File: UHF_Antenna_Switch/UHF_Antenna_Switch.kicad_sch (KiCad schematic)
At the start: 27 parts, among them J1 Conn_N_Type_Female, J2 Conn_SO-239, J3 Conn_SMA_Female, J4 Screw_Terminal_01x02, SW1 SW_SP3T, U1 LTC5507ES6, U2 PAT1220-C-10DB, U3 X4C09F1-30S, U4 RP2040-Zero

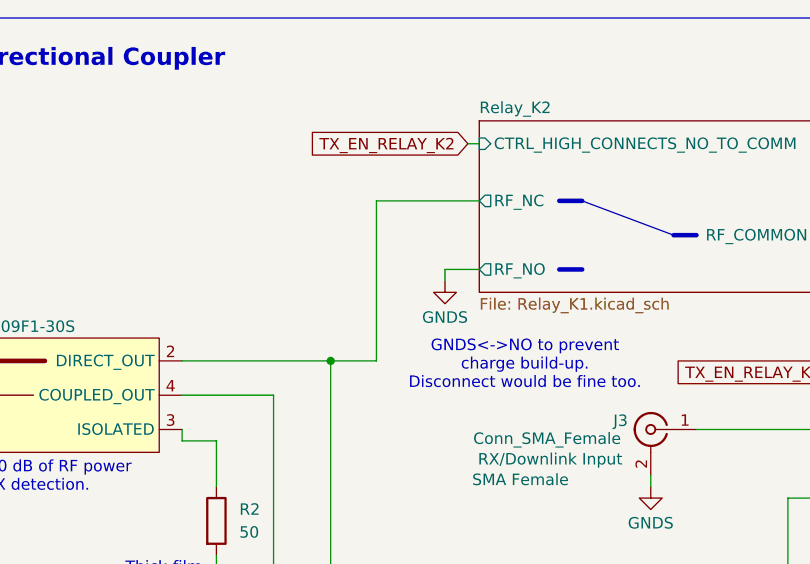
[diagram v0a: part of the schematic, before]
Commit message: Configure net classes and trace widths
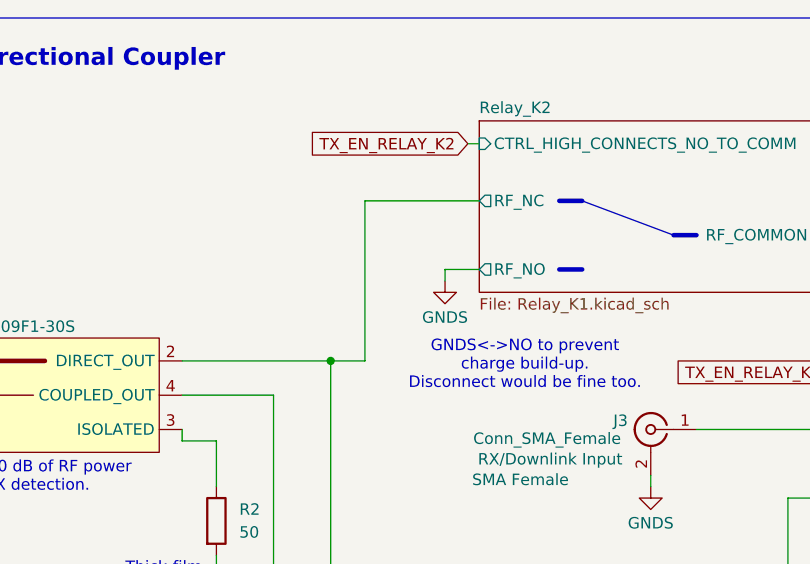
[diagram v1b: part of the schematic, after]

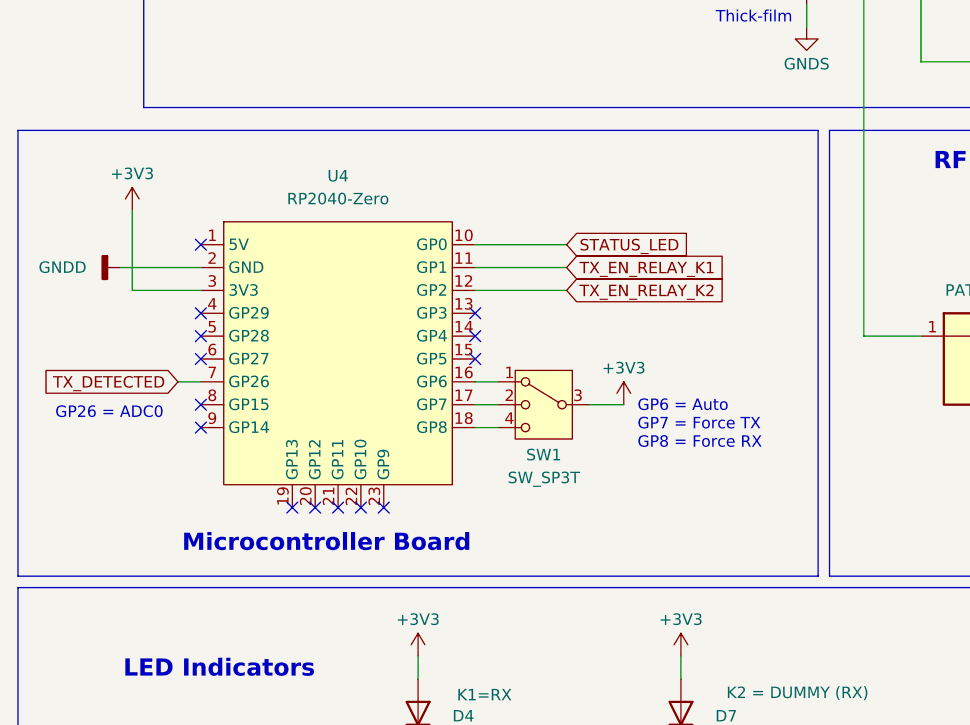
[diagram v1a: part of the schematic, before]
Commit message: Complete initial positioning of components (no routing)
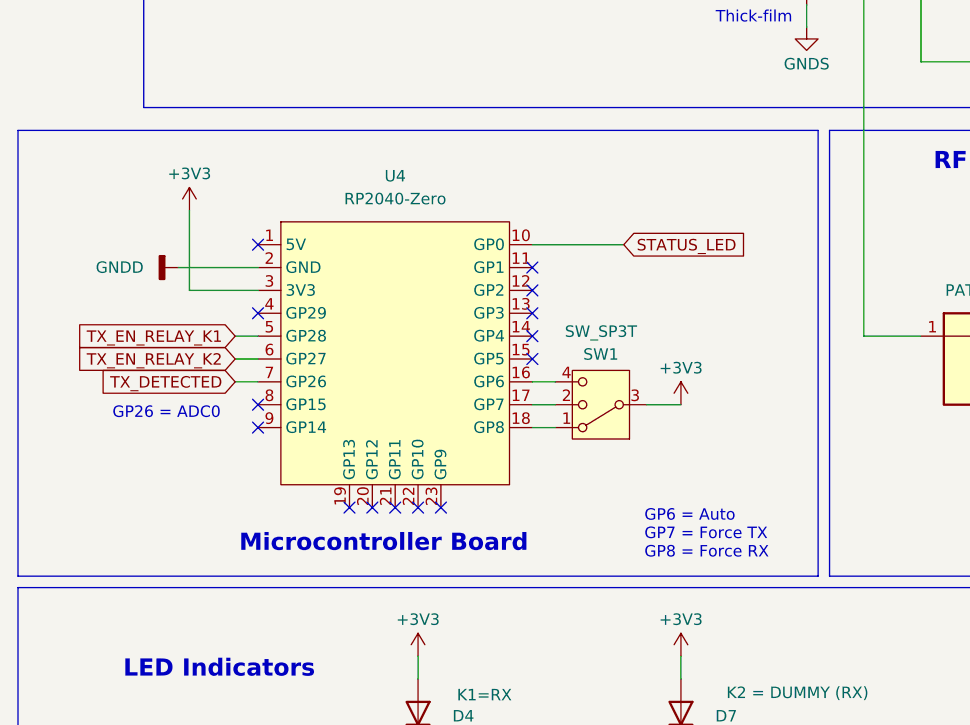
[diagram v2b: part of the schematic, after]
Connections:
- net TX_EN_RELAY_K1: now also U4.5 (GP28); no longer U4.11 (GP1)
- net TX_EN_RELAY_K2: now also U4.6 (GP27); no longer U4.12 (GP2)
- net at U4.16 (GP6): now also SW1.4; no longer SW1.1
- net at U4.18 (GP8): now also SW1.1; no longer SW1.4
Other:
- moved on the sheet: SW1, U4

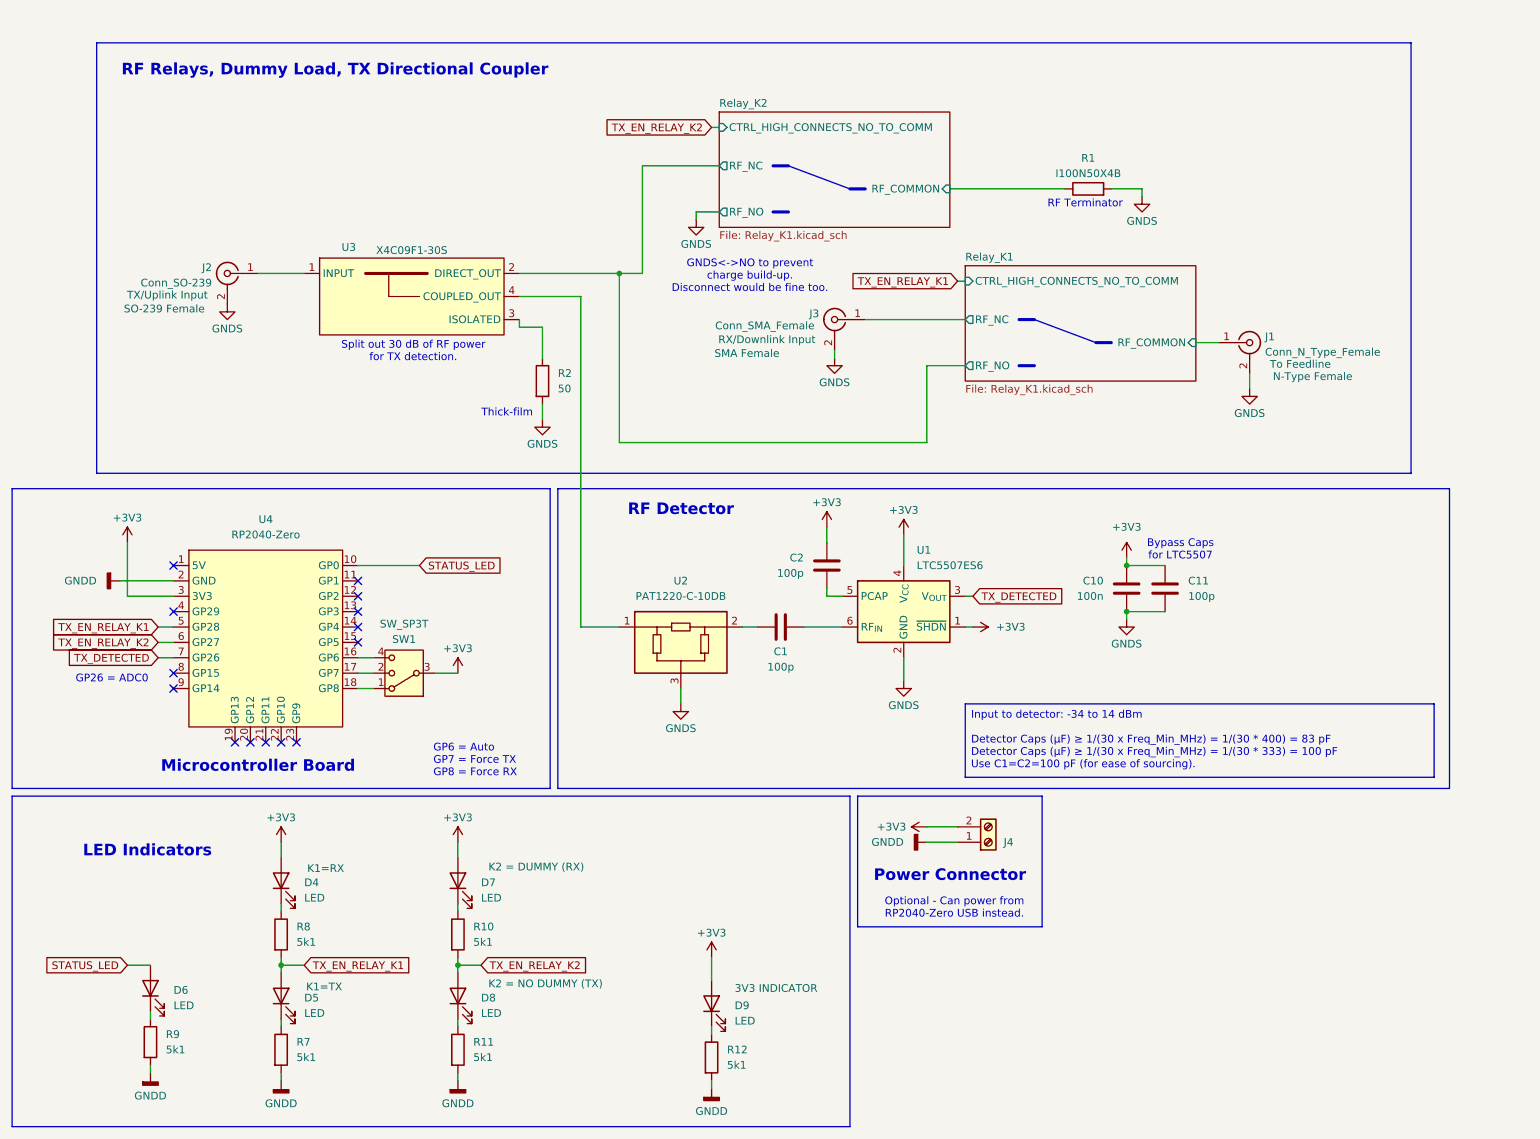
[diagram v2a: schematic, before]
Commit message: Schematic: Add PTT switches, PTT header, 5V power screw
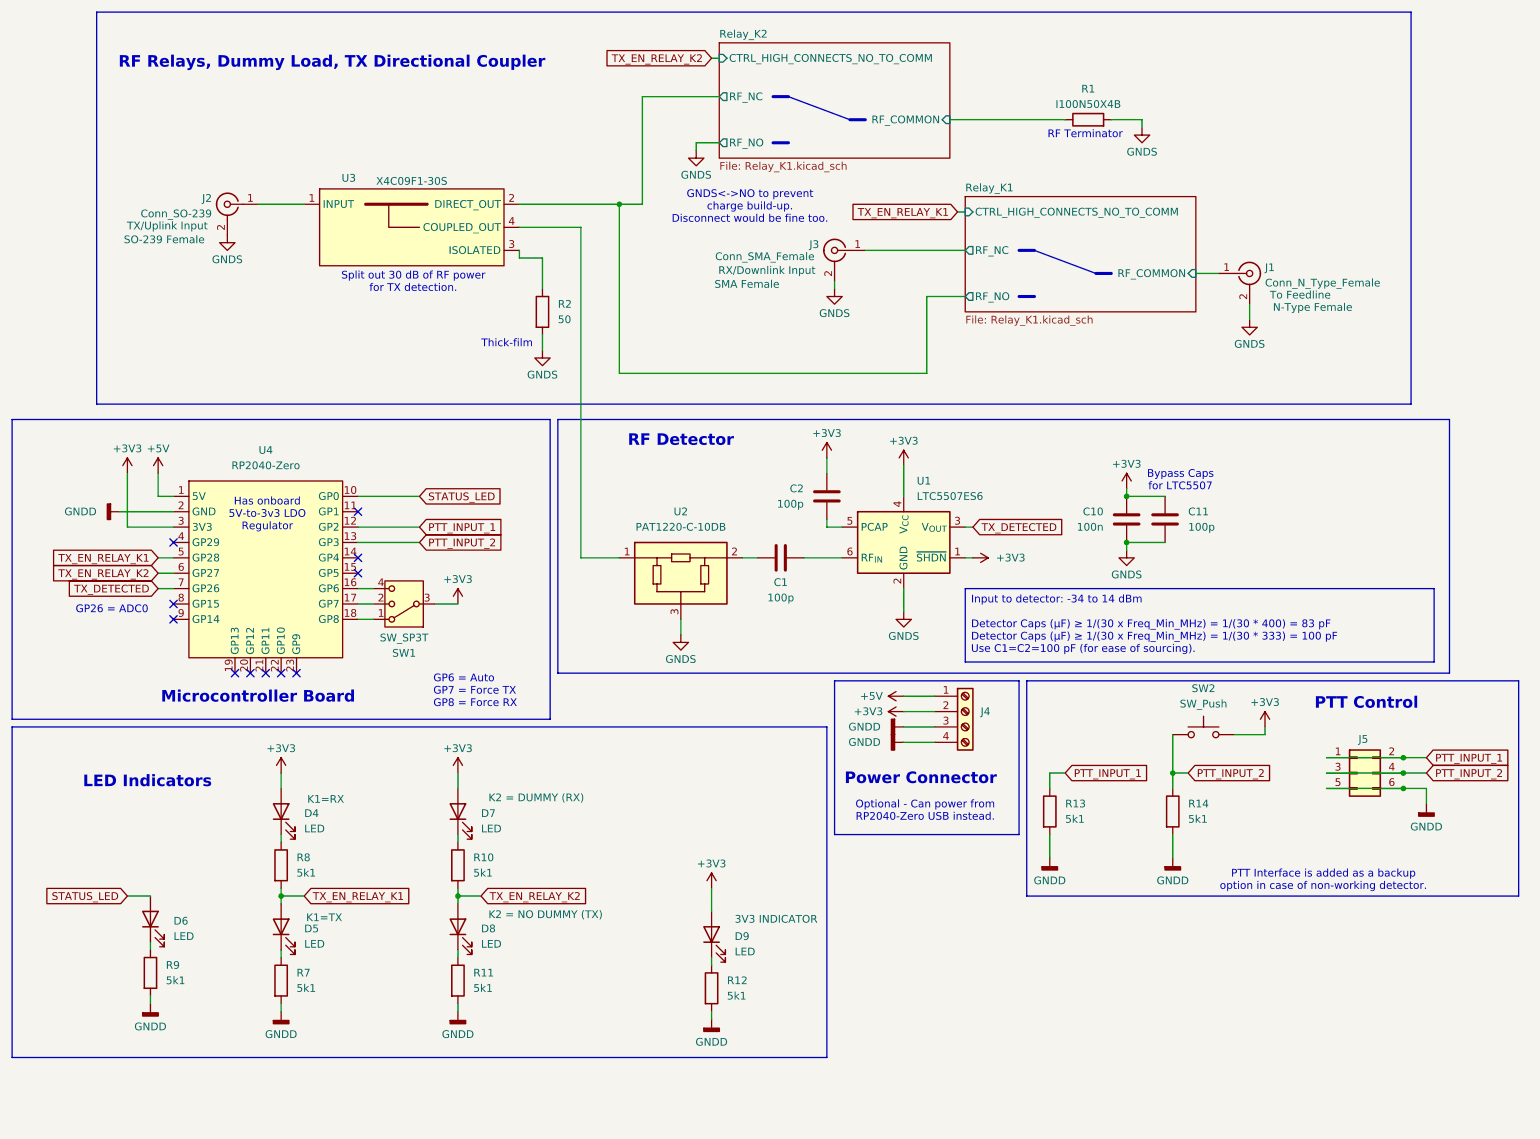
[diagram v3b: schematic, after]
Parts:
- removed J4: Screw_Terminal_01x02, TerminalBlock_Phoenix:TerminalBlock_Phoenix_MKDS-3-2-5.08_1x02_P5.08mm_Horizontal, symbol Connector:Screw_Terminal_01x02
- added J4: Screw_Terminal_01x04, TerminalBlock_Phoenix:TerminalBlock_Phoenix_MKDS-1,5-4-5.08_1x04_P5.08mm_Horizontal, symbol Connector:Screw_Terminal_01x04
- added J5: Conn_02x03_Odd_Even, Connector_PinHeader_2.54mm:PinHeader_2x03_P2.54mm_Vertical, symbol Connector_Generic:Conn_02x03_Odd_Even
- added R13, R14: 5k1, Resistor_SMD:R_0603_1608Metric_Pad0.98x0.95mm_HandSolder, symbol Device:R
- added SW2: SW_Push, Button_Switch_THT:SW_PUSH_6mm_H4.3mm, symbol Switch:SW_Push
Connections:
- net +3V3: now also J4.2 (Pin_2), SW2.2
- net GNDD: now also J4.3 (Pin_3), J4.4 (Pin_4), J5.5 (Pin_5), J5.6 (Pin_6), R13.2, R14.2
- net +5V: now reaches U4.1 (5V)
- net +5V: now also J4.1 (Pin_1)
- net PTT_INPUT_1: now reaches U4.12 (GP2)
- net PTT_INPUT_1: now also J5.1 (Pin_1), J5.2 (Pin_2), R13.1
- net PTT_INPUT_2: now reaches U4.13 (GP3)
- net PTT_INPUT_2: now also J5.3 (Pin_3), J5.4 (Pin_4), R14.1, SW2.1
- no-connect marks 14 -> 11
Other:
- note added: "Has onboard 5V-to-3v3 LDO Regulator"
- note added: "PTT Control"
- note added: "PTT Interface is added as a backup option in case of non-working detector."
- moved on the sheet: C1, C10, C11, C2, D4, D5, D6, D7, D8, D9, J1, J2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

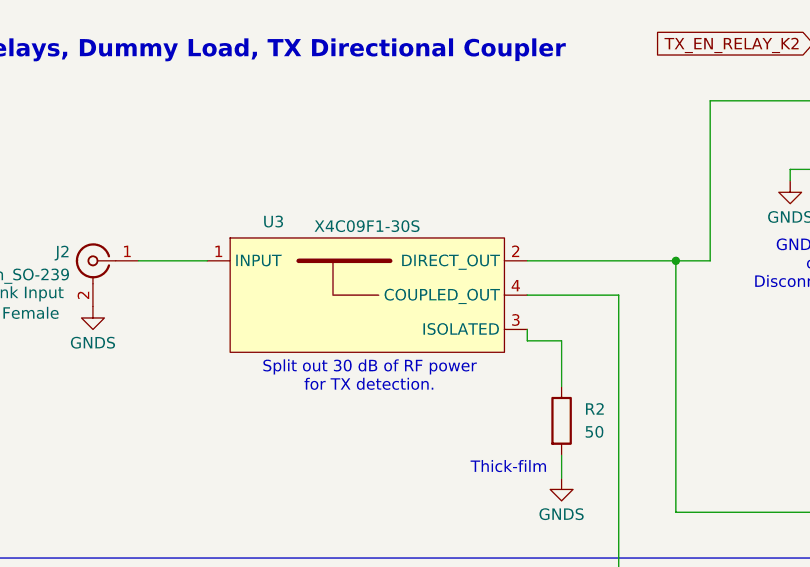
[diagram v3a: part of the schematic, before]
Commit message: Footprint: Draw RF coupler with microstrip
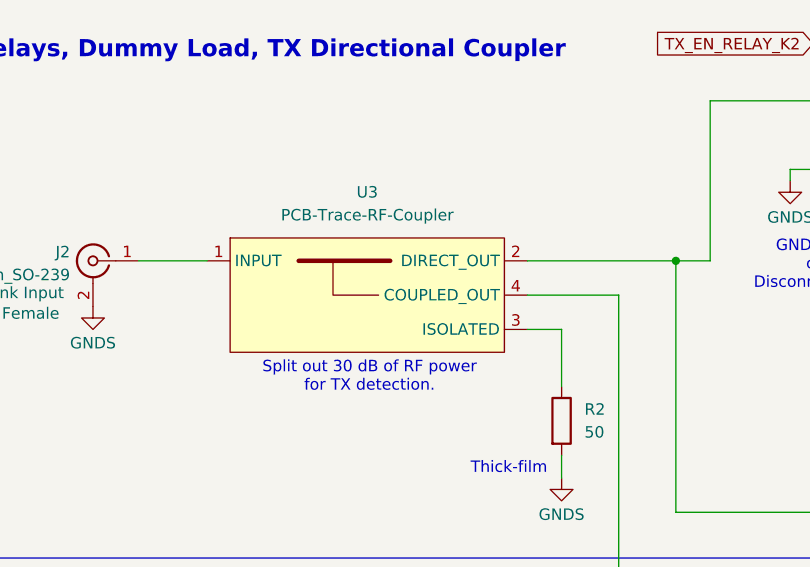
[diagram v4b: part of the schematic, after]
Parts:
- removed U3: X4C09F1-30S, 00-project-footprints:X4C09F1-30S, symbol 00-project-symbols:X4C09F1-30S
- added U3: PCB-Trace-RF-Coupler, 00-project-footprints:PCB-Trace-RF-Coupler, symbol 00-project-symbols:PCB-Trace-RF-Coupler
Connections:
- net Relay_K1/RF_NO: now also U3.2 (DIRECT_OUT)
- net at U2.1: now also U3.4 (COUPLED_OUT)
- net at J2.1 (In): now also U3.1 (INPUT)
- net at R2.1: now also U3.3 (ISOLATED)
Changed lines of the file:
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@@
 	(wire
 		(pts
-			(xy 97.79 53.34) (xy 97.79 54.61)
-		)
-		(stroke
-			(width 0)
-			(type default)
-		)
-	)
-	(wire
-		(pts
 			(xy 71.12 114.3) (xy 73.66 114.3)
 		)
@@
 	(wire
 		(pts
-			(xy 97.79 54.61) (xy 101.6 54.61)
+			(xy 97.79 53.34) (xy 101.6 53.34)
 		)
 		(stroke
@@
 	(wire
 		(pts
-			(xy 101.6 54.61) (xy 101.6 59.69)
+			(xy 101.6 53.34) (xy 101.6 59.69)
 		)
 		(stroke
@@
 		(length 2.54)
 		(shape round)
-		(at 62.23 45.72 0)
+		(at 60.96 45.72 0)
 		(effects
 			(font
@@
 		)
 		(property "Net Class" "50_Ohm_RF"
-			(at 62.992 41.402 0)
+			(at 61.722 41.402 0)
 			(show_name no)
 			(do_not_autoplace no)
@@
 		)
 		(property "Component Class" ""
-			(at 135.89 -2.54 0)
+			(at 134.62 -2.54 0)
 			(show_name no)
 			(do_not_autoplace no)
@@
 	)
 	(symbol
+		(lib_id "00-project-symbols:PCB-Trace-RF-Coupler")
+		(at 80.01 46.99 0)
+		(unit 1)
+		(body_style 1)
+		(exclude_from_sim no)
+		(in_bom yes)
+		(on_board yes)
+		(in_pos_files yes)
+		(dnp no)
+		(fields_autoplaced yes)
+		(property "Reference" "U3"
+			(at 80.01 38.1 0)
+			(show_name no)
+			(do_not_autoplace no)
+			(effects
+				(font
+					(size 1.27 1.27)
+				)
+			)
+		)
+		(property "Value" "PCB-Trace-RF-Coupler"
+			(at 80.01 40.64 0)
+			(show_name no)
+			(do_not_autoplace no)
+			(effects
+				(font
+					(size 1.27 1.27)
+				)
+			)
+		)
+		(property "Footprint" "00-project-footprints:PCB-Trace-RF-Coupler"
+			(at 80.01 46.99 0)
+			(hide yes)
+			(show_name no)
+			(do_not_autoplace no)
+			(effects
+				(font
+					(size 1.27 1.27)
+				)
+			)
+		)
+		(property "Datasheet" ""
+			(at 80.264 58.674 0)
+			(hide yes)
+			(show_name no)
+			(do_not_autoplace no)
+			(effects
+				(font
+					(size 1.27 1.27)
+				)
+			)
+		)
+		(property "Description" ""
+			(at 78.486 61.722 0)
+			(hide yes)
+			(show_name no)
+			(do_not_autoplace no)
+			(effects
+				(font
+					(size 1.27 1.27)
+				)
+			)
+		)
+		(pin "3"
+		)
+		(pin "1"
+		)
+		(pin "2"
+		)
+		(pin "4"
+		)
+		(instances
+			(project "UHF_Antenna_Switch"
+				(path "/0ffb5503-f768-4a51-945c-501d4ddb5b7c"
+					(reference "U3")
+					(unit 1)
+				)
+			)
+		)
+	)
+	(symbol
 		(lib_id "Connector:Conn_Coaxial")
 		(at 149.86 53.34 0)
@@
 					(unit 1)
 				)
-			)
-		)
-	)
-	(symbol
-		(lib_id "00-project-symbols:X4C09F1-30S")
-		(at 80.01 46.99 0)
-		(unit 1)
-		(body_style 1)
-		(exclude_from_sim no)
-		(in_bom yes)
-		(on_board yes)
-		(in_pos_files yes)
-		(dnp no)
-		(property "Reference" "U3"
-			(at 69.596 41.402 0)
-			(show_name no)
-			(do_not_autoplace no)
-			(effects
-				(font
-					(size 1.27 1.27)
-				)
-			)
-		)
-		(property "Value" "X4C09F1-30S"
-			(at 80.01 41.91 0)
-			(show_name no)
-			(do_not_autoplace no)
-			(effects
-				(font
-					(size 1.27 1.27)
-				)
-			)
-		)
-		(property "Footprint" "00-project-footprints:X4C09F1-30S"
-			(at 80.01 46.99 0)
-			(hide yes)
-			(show_name no)
-			(do_not_autoplace no)
-			(effects
-				(font
-					(size 1.27 1.27)
-				)
-			)
-		)
-		(property "Datasheet" "https://cdn.ttm.com/repository/products/wireless-xinger/10-20-30-dB-directional-couplers/X4C09F1-30S/X4C09F1-30S.pdf"
-			(at 80.264 58.674 0)
-			(hide yes)
-			(show_name no)
-			(do_not_autoplace no)
-			(effects
-				(font
-					(size 1.27 1.27)
-				)
-			)
-		)
-		(property "Description" "RF Directional Coupler AMPS, GSM, LTE, WCDMA 400MHz ~ 1GHz 30dB 100W 4-SMD, No Lead"
-			(at 78.486 61.722 0)
-			(hide yes)
-			(show_name no)
-			(do_not_autoplace no)
-			(effects
-				(font
-					(size 1.27 1.27)
-				)
-			)
-		)
-		(pin "4"
-		)
-		(pin "1"
-		)
-		(pin "3"
-		)
-		(pin "2"
-		)
-		(instances
-			(project "UHF_Antenna_Switch"
-				(path "/0ffb5503-f768-4a51-945c-501d4ddb5b7c"
-					(reference "U3")
-					(unit 1)
-				)
